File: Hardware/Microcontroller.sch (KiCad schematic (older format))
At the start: 20 parts

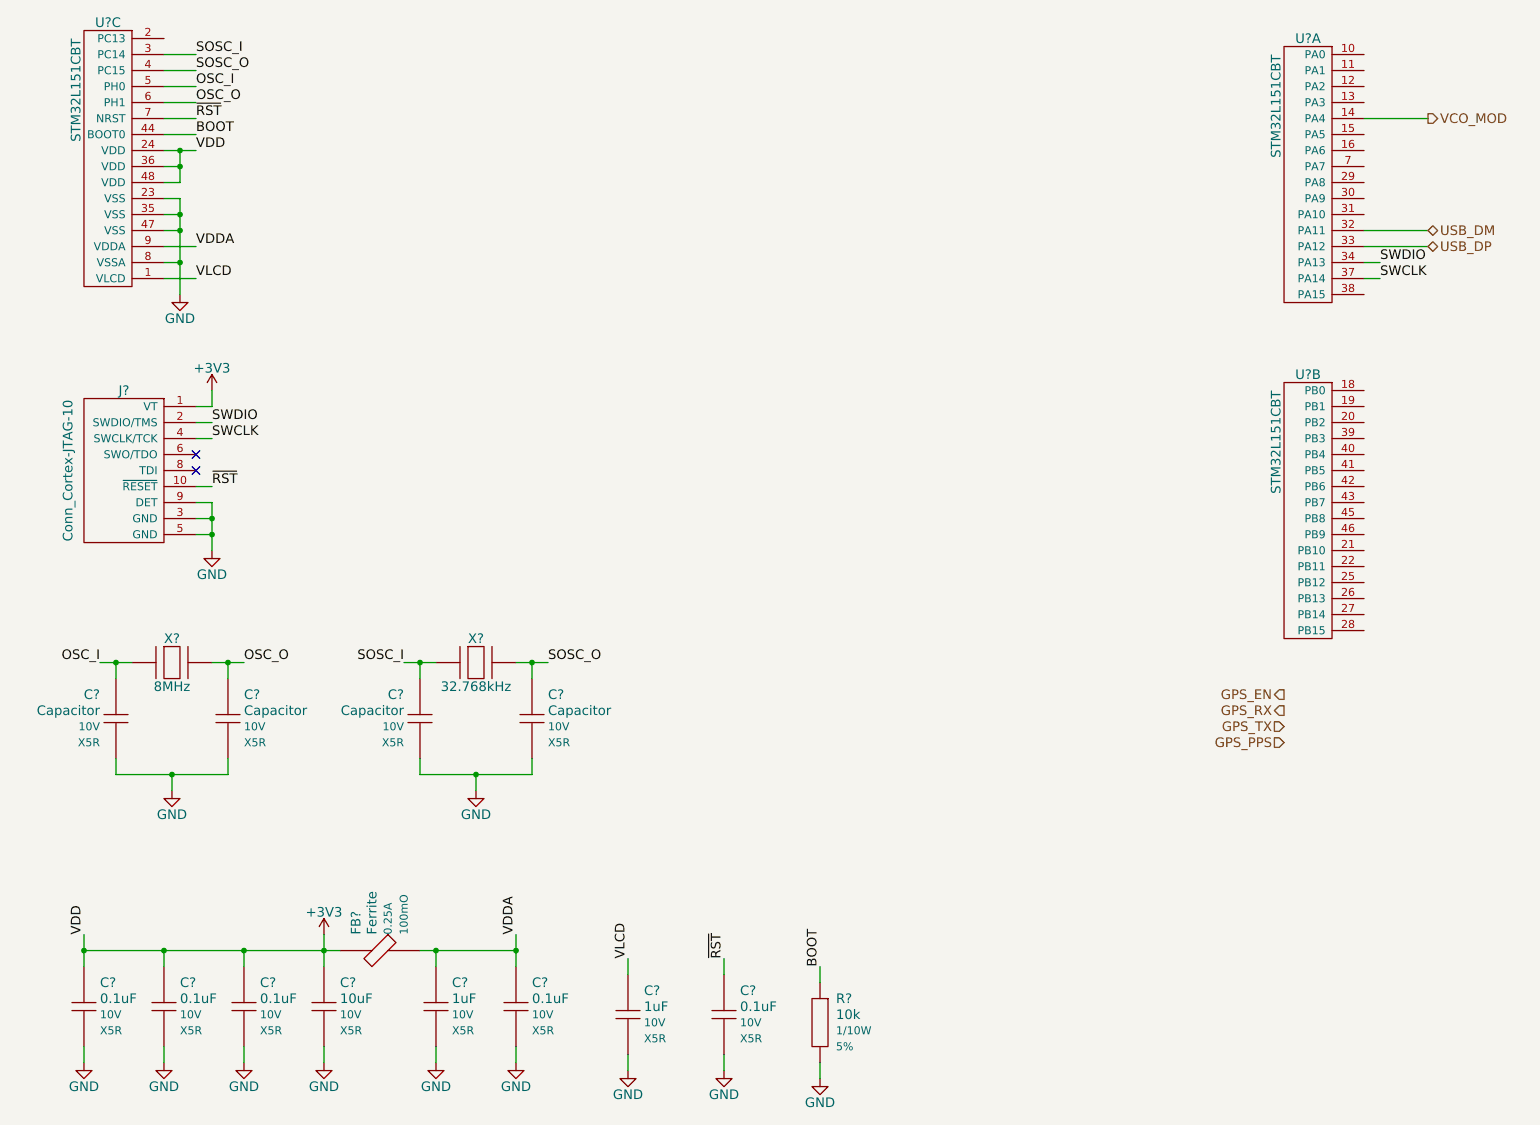
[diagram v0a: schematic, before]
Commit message: USB circuitry
Closes #27
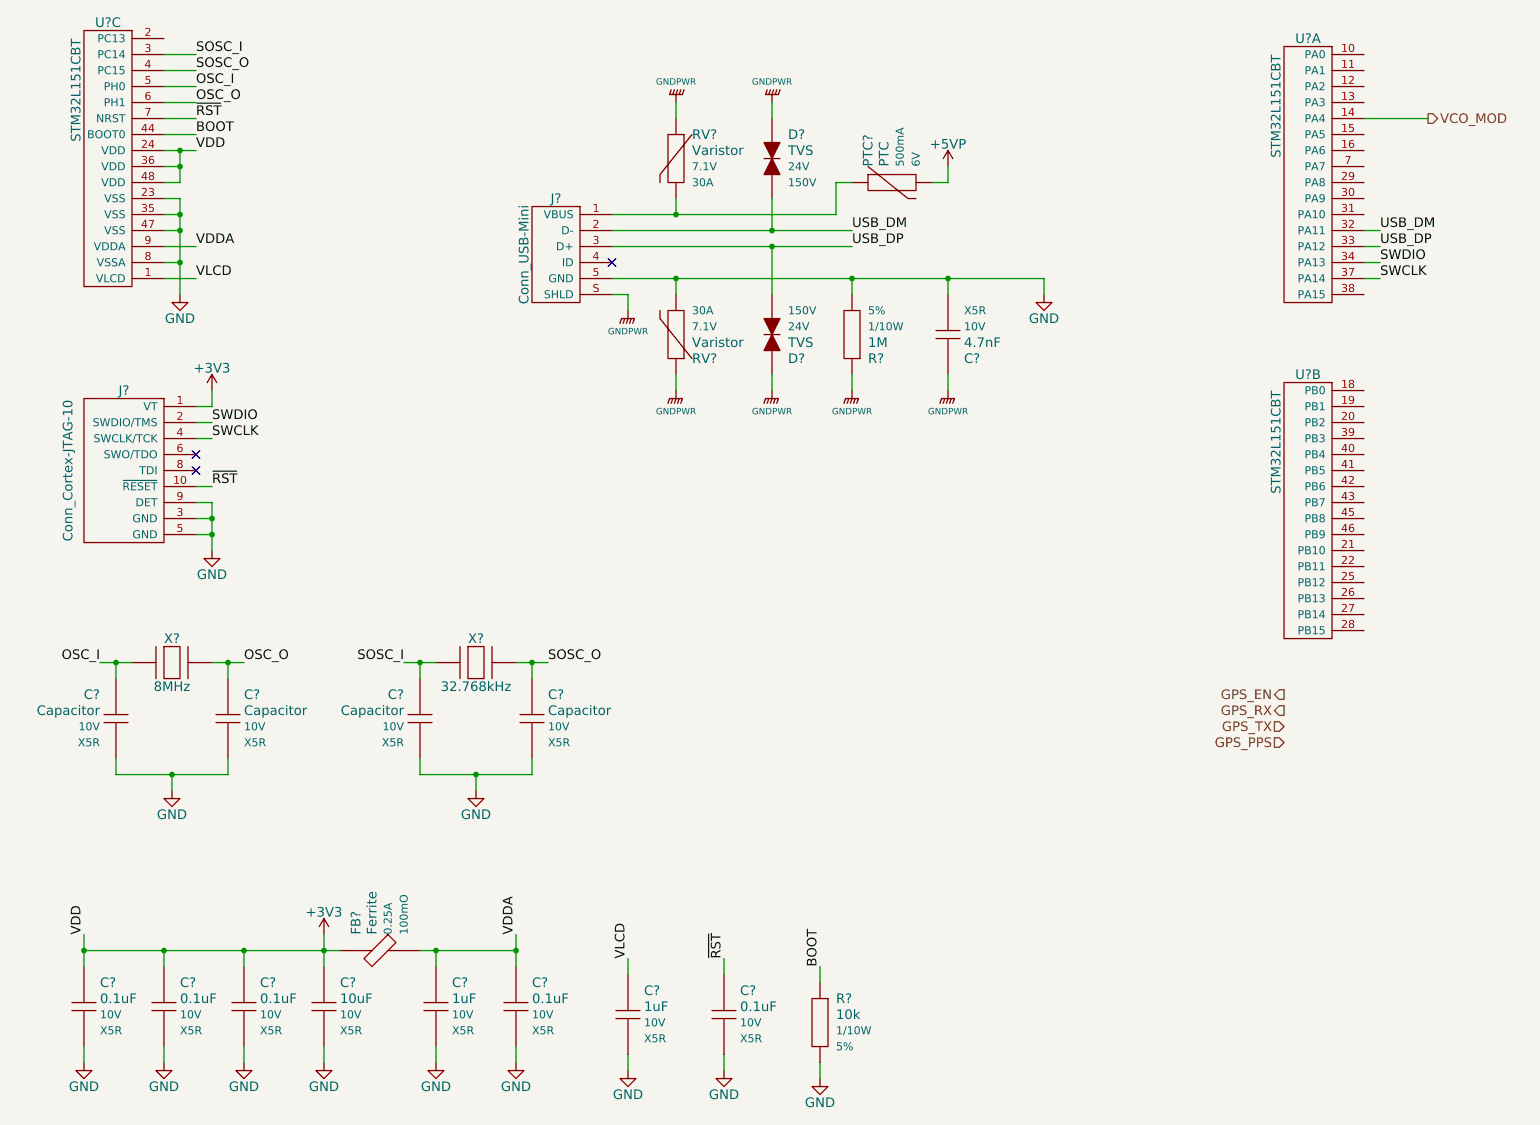
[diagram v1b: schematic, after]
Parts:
- added C?: 4.7nF, symbol Capacitor
- added D? (x2): TVS, symbol TVS
- added J?: Conn_USB-Mini, symbol Conn_USB-Mini
- added PTC?: PTC, symbol PTC
- added R?: 1M, symbol Resistor
- added RV? (x2): Varistor, symbol Varistor
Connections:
- net GND: now also C?.2, J?.5 (GND), R?.2, RV?.2
- net USB_DM: now also D?.2, J?.2 (D-)
- net USB_DP: now also D?.2, J?.3 (D+)
- new net: J?.1 (VBUS), PTC?.1, RV?.2
- new net +5VP: PTC?.2
- new net GNDPWR: C?.1, D?.1, D?.1, J?.S (SHLD), R?.1, RV?.1, RV?.1
- no-connect marks 2 -> 3

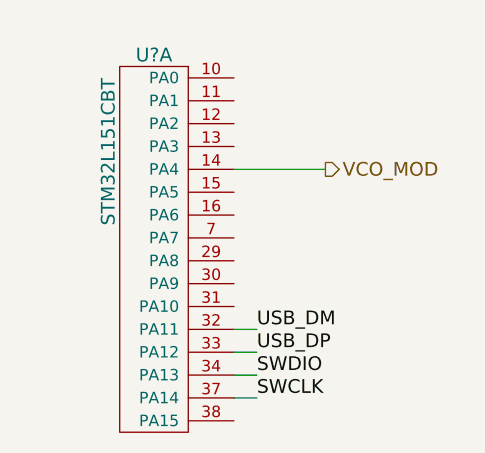
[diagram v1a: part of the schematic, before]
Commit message: Rough TCVR circuitry
First order TX topology #28
Core circuitry for TCVR, closes #23
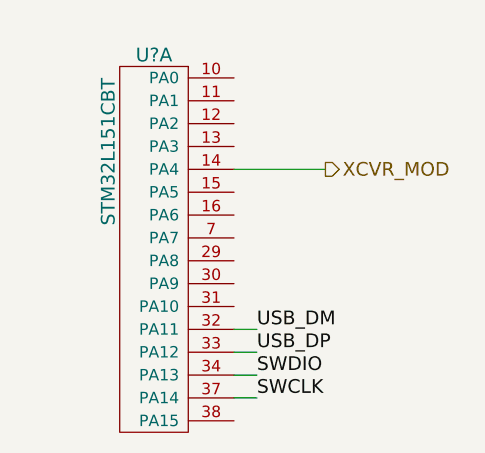
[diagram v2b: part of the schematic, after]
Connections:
- net VCO_MOD renamed XCVR_MOD
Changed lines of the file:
@@
 $Descr A4 11693 8268
 encoding utf-8
-Sheet 3 3
+Sheet 3 4
 Title ""
 Date ""
@@
 	1500 1100 1700 1100
 Text HLabel 9400 1400 2    60   Output ~ 0
-VCO_MOD
+XCVR_MOD
 Wire Wire Line
 	9400 1400 9000 1400
